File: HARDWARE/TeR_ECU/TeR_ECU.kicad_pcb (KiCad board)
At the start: 2 copper layers, 71 parts, among them IC1 MX34040NF2, J1 RJ45_Shielded, J2 RJ45_Shielded, J3 RJ45_Shielded, J4 Debug, Q1 ZXMN3F30FH, Q2 ZXMN3F30FH, SW1 RST, U1 SN65HVD230, U2 SN65HVD230, U3 STM32F446RETx, U4 TSR_1-24120, U5 TSR_1-2450, U6 LM1117MP-3.3, Y1 Crystal

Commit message: Latout empezado
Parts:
- moved IC1 163.1 mm to (160.7, 140.3)
- moved U3 130.2 mm to (151.7, 99.4)
- moved F1 128.8 mm to (190.7, 44.4)
- moved L2 128.5 mm to (187.6, 40.5)
- moved C18 128.5 mm to (186.0, 48.0)
- moved C19 128.5 mm to (186.0, 51.0)
- moved U2 88.0 mm to (126.5, 88.1), turned to 180 degrees
- moved JP2 82.0 mm to (120.5, 88.0), turned to 90 degrees
- moved R3 78.6 mm to (116.8, 90.0)
- moved D2 76.7 mm to (112.3, 88.4), turned to 180 degrees
- moved C4 74.0 mm to (124.8, 84.2)
- moved R4 72.8 mm to (116.6, 86.2), turned to 180 degrees
- moved U4 71.8 mm to (119.0, 53.5)
- moved J1 66.1 mm to (116.3, 130.0)
- moved J2 65.1 mm to (103.2, 110.3), turned to -90 degrees
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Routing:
- net +24V: track 0.00 -> 84.6 mm
- net /CAN2/CAN-: track 0.00 -> 22.6 mm
- net /CAN2/CAN+: track 0.00 -> 20.3 mm
- net GND: track 0.00 -> 14.3 mm, vias 0 -> 4
- net /CAN2/VREF: track 0.00 -> 12.4 mm, vias 0 -> 2
- net Net-(U5-Vin): track 0.00 -> 9.43 mm
- net +3.3V: track 0.00 -> 9.16 mm
- net Net-(C22-Pad1): track 0.00 -> 5.54 mm
- net Net-(JP2-B): track 0.00 -> 3.57 mm
- net Net-(JP2-A): track 0.00 -> 3.11 mm
- net +5V: track 0.00 -> 2.83 mm
- added copper zone on In1.Cu, net GND
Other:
- copper layers 2 -> 4

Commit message: Contuinuando con Layout, micro hecha
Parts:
- moved C8 148.5 mm to (155.9, 107.7)
- moved C9 147.9 mm to (159.9, 94.9), turned to 90 degrees
- moved C6 142.9 mm to (147.6, 107.5)
- moved C16 134.3 mm to (147.5, 90.9), turned to 180 degrees
- moved C5 134.1 mm to (143.4, 90.7), turned to -90 degrees
- moved C7 134.1 mm to (143.7, 95.8), turned to 90 degrees
- moved J4 127.5 mm to (159.4, 90.3), turned to -90 degrees
- moved C15 123.9 mm to (136.5, 96.3), turned to -90 degrees
- moved C14 123.5 mm to (136.5, 92.5), turned to -90 degrees
- moved FB1 122.0 mm to (142.1, 103.5), turned to -90 degrees
- moved R8 120.2 mm to (141.2, 98.6), turned to 180 degrees
- moved C10 118.2 mm to (143.6, 101.4), turned to -90 degrees
- moved C11 114.3 mm to (139.8, 102.4)
- moved C12 114.0 mm to (139.8, 103.6)
- moved Y1 107.0 mm to (139.7, 94.7), turned to -90 degrees
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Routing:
- net GND: track 14.3 -> 40.4 mm, vias 4 -> 9
- net +3.3V: track 9.16 -> 34.8 mm, vias 0 -> 2
- net /Micro/OSC_IN: track 0.00 -> 13.9 mm
- net +24V: track 84.6 -> 93.2 mm
- net /Micro/SWDIO: track 0.00 -> 7.99 mm
- net Net-(C15-Pad2): track 0.00 -> 6.14 mm
- net +3.3VADC: track 0.00 -> 6.00 mm
- net /Micro/OSC_OUT: track 0.00 -> 4.50 mm
- net /Micro/SWCLK: track 0.00 -> 3.45 mm
- added copper zone on In2.Cu, net +3.3V
- added copper zone on In2.Cu, net +5V
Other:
- board text added: "DBUG"

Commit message: Seguir Layout, falta señales
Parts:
- moved R7 150.5 mm to (166.6, 96.0), turned to 180 degrees
- moved R6 149.2 mm to (166.6, 87.4), turned to 180 degrees
- moved JP3 147.5 mm to (169.4, 90.1), turned to -90 degrees
- moved JP4 144.2 mm to (169.4, 93.5), turned to -90 degrees
- moved C13 125.9 mm to (133.7, 103.0), turned to 90 degrees
- moved R5 121.5 mm to (133.7, 99.4), turned to -90 degrees
- moved U1 100.6 mm to (125.4, 109.4), turned to 180 degrees
- moved SW1 99.8 mm to (130.4, 101.2), turned to 90 degrees
- moved C1 97.4 mm to (130.4, 109.5), turned to 90 degrees
- moved JP1 88.6 mm to (119.3, 109.4), turned to 90 degrees
- moved R1 87.8 mm to (115.7, 111.4)
- moved C3 87.4 mm to (121.7, 105.4), turned to 180 degrees
- moved D1 87.2 mm to (111.2, 109.3), turned to 180 degrees
- moved R2 85.8 mm to (115.6, 107.4), turned to 180 degrees
- moved C2 82.0 mm to (131.2, 86.8), turned to 90 degrees
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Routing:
- net /DBG_LED: track 0.00 -> 33.6 mm, vias 0 -> 2
- net +24V: track 93.2 -> 59.7 mm
- net +3.3V: track 34.8 -> 67.9 mm, vias 2 -> 9
- net GND: track 40.4 -> 72.4 mm, vias 9 -> 15
- net /IMP_LED: track 0.00 -> 30.7 mm, vias 0 -> 2
- net /CAN1/CAN-: track 0.00 -> 23.0 mm
- net /Micro/BOOT0: track 0.00 -> 22.0 mm, vias 0 -> 2
- net /CAN1/CAN+: track 0.00 -> 21.0 mm
- net /Micro/NRST: track 0.00 -> 19.1 mm, vias 0 -> 2
- net /Micro/BOOT1: track 0.00 -> 17.6 mm, vias 0 -> 2
- net /CAN1/VREF: track 0.00 -> 16.6 mm, vias 0 -> 2
- net Net-(SW1-B): track 0.00 -> 3.76 mm
- net Net-(JP1-B): track 0.00 -> 3.08 mm
- net Net-(JP1-A): track 0.00 -> 2.98 mm
- net Net-(JP3-C): track 0.00 -> 2.71 mm
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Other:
- board text added: "BOOT0"
- board text added: "BOOT1"

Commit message: avanzando
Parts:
- moved R13 140.8 mm to (152.6, 112.0), turned to 90 degrees
- moved Q1 140.2 mm to (156.3, 114.2)
- moved R14 134.6 mm to (145.4, 117.5)
- moved Q2 134.6 mm to (150.0, 120.0)
- moved R15 134.5 mm to (145.4, 120.5)
- moved R16 134.5 mm to (145.4, 123.3)
- moved R17 134.4 mm to (145.4, 125.8)
- moved R9 115.5 mm to (164.2, 99.3), turned to 180 degrees
- moved R11 113.6 mm to (164.3, 102.0), turned to 180 degrees
- moved R10 110.6 mm to (161.0, 98.5), turned to 90 degrees
- moved R12 109.1 mm to (160.8, 102.2), turned to -90 degrees
- moved L2 57.8 mm to (138.0, 70.1)
- moved F1 53.0 mm to (144.4, 70.2), turned to 180 degrees
- moved C19 52.3 mm to (135.8, 65.6), turned to 90 degrees
- moved C18 49.2 mm to (140.1, 65.5), turned to 90 degrees
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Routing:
- net GND: track 72.4 -> 82.0 mm, vias 15 -> 18
- net Net-(U4-Vin): track 0.00 -> 8.62 mm
- net Net-(C18-Pad1): track 0.00 -> 7.05 mm
- net /Micro/BOOT1: track 17.6 -> 24.5 mm
- net /Detección señales/BSPD_3V3: track 0.00 -> 6.77 mm
- net /Detección señales/TSMS_3V3: track 0.00 -> 6.07 mm
- net /Micro/BOOT0: track 22.0 -> 19.1 mm

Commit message: Falta poco
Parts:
- moved C21 58.5 mm to (121.5, 127.8), turned to -90 degrees
- moved U4 56.7 mm to (145.9, 123.8), turned to 180 degrees
- moved U6 54.8 mm to (115.8, 126.2), turned to 180 degrees
- moved C19 54.6 mm to (148.4, 118.8), turned to 0 degrees
- moved C18 53.2 mm to (137.7, 118.7), turned to 180 degrees
- moved C17 52.2 mm to (124.7, 123.8), turned to -90 degrees
- moved C20 51.1 mm to (121.5, 124.0), turned to -90 degrees
- moved L2 49.0 mm to (143.1, 118.8), turned to 180 degrees
- moved U5 48.6 mm to (128.4, 120.3), turned to -90 degrees
- moved R17 48.0 mm to (171.3, 85.3)
- moved R16 47.9 mm to (171.4, 83.0)
- moved R15 44.9 mm to (157.4, 77.3), turned to 180 degrees
- moved C22 44.8 mm to (115.4, 121.2), turned to 180 degrees
- moved F1 44.2 mm to (142.1, 114.3)
- moved L1 41.7 mm to (121.5, 119.2), turned to 180 degrees
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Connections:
- U3 pad 24: unconnected-(U3-PC4-Pad24) -> /Functions/BL
- U3 pad 25: unconnected-(U3-PC5-Pad25) -> /Functions/Horn
- U3 pad 52: /Functions/BL -> unconnected-(U3-PC11-Pad52)
- U3 pad 53: /Functions/Horn -> unconnected-(U3-PC12-Pad53)
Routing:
- net /CAN1/CAN-: track 23.0 -> 87.3 mm
- net /CAN1/CAN+: track 21.0 -> 77.2 mm
- net +24V: track 59.7 -> 23.5 mm, vias 0 -> 1
- net Net-(Q1-G): track 0.00 -> 7.77 mm
- net /Functions/Horn: track 0.00 -> 5.68 mm
- net /DBG_LED: track 33.6 -> 36.7 mm
- net /IMP_LED: track 30.7 -> 33.8 mm
- net /Micro/NRST: track 19.1 -> 21.4 mm
- net GND: track 82.0 -> 84.2 mm, vias 18 -> 19
- net Net-(U4-Vin): track 8.62 -> 7.57 mm
- net +3.3V: track 67.5 -> 67.7 mm, vias 9 -> 10
- added copper zone on In2.Cu, net +24V

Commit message: Falta Conector
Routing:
- net /CAN1/CAN_TX: track 0.00 -> 36.1 mm
- net /CAN1/CAN_RX: track 0.00 -> 34.1 mm, vias 0 -> 2
- net +24V: track 23.5 -> 56.6 mm
- net GND: track 84.2 -> 102.8 mm, vias 19 -> 27
- net +5V: track 2.83 -> 5.46 mm, vias 0 -> 1
- net /Micro/BOOT1: track 24.5 -> 23.5 mm
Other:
- board text added: "CAN+"
- board text added: "CAN-"

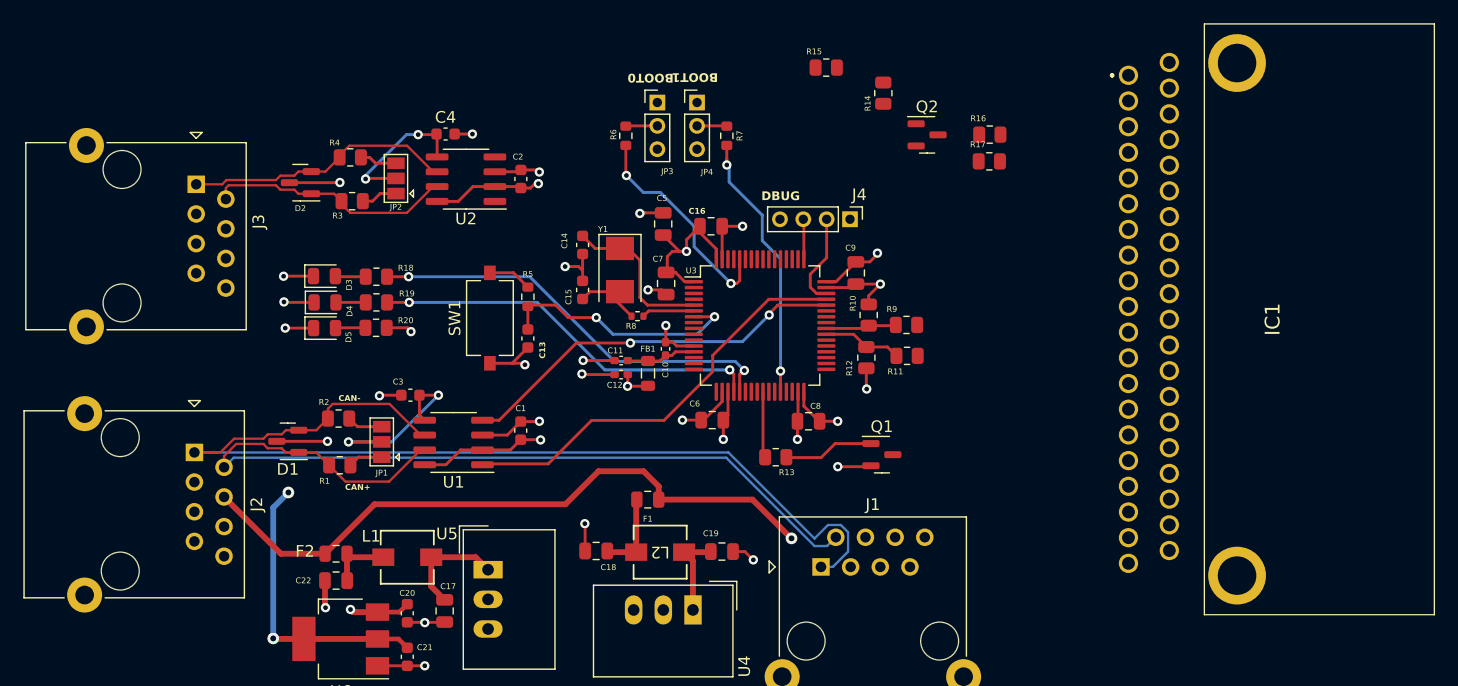
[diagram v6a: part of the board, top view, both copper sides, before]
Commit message: Falta pinear conector
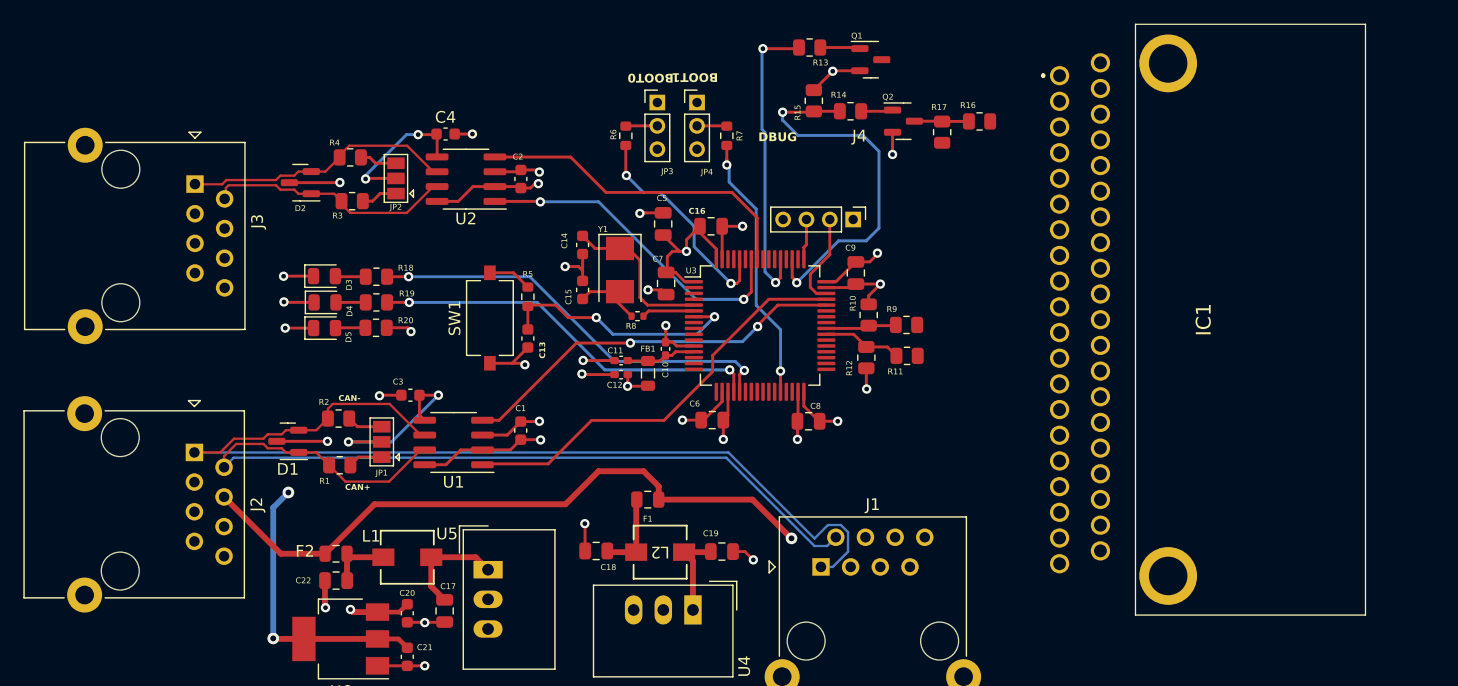
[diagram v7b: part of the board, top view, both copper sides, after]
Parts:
- moved R13 35.2 mm to (155.9, 75.6)
- moved Q1 33.8 mm to (161.2, 76.6)
- moved IC1 5.90 mm to (189.7, 98.9)
- moved R17 4.75 mm to (167.3, 82.8), turned to -90 degrees
- moved R14 3.21 mm to (159.4, 81.0), turned to 180 degrees
- moved R15 3.03 mm to (156.3, 80.2), turned to 90 degrees
- moved Q2 2.34 mm to (164.0, 81.9)
- moved R16 1.43 mm to (170.5, 81.9)
- moved J4 0.27 mm to (159.7, 90.3)
- moved J3 0.11 mm to (103.3, 87.3)
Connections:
- U3 pad 24: /Functions/BL -> unconnected-(U3-PC4-Pad24)
- U3 pad 25: /Functions/Horn -> unconnected-(U3-PC5-Pad25)
- U3 pad 33: /CAN2/CAN_TX -> unconnected-(U3-PB12-Pad33)
- U3 pad 34: /CAN2/CAN_RX -> unconnected-(U3-PB13-Pad34)
- U3 pad 51: unconnected-(U3-PC10-Pad51) -> /Functions/BL
- U3 pad 53: unconnected-(U3-PC12-Pad53) -> /Functions/Horn
- U3 pad 57: unconnected-(U3-PB5-Pad57) -> /CAN2/CAN_RX
- U3 pad 58: unconnected-(U3-PB6-Pad58) -> /CAN2/CAN_TX
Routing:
- net /Functions/BL: track 0.00 -> 33.1 mm, vias 0 -> 2
- net /CAN2/CAN_TX: track 0.00 -> 28.6 mm, vias 0 -> 2
- net /CAN2/CAN_RX: track 0.00 -> 28.2 mm
- net /Functions/Horn: track 5.68 -> 25.9 mm, vias 0 -> 2
- net Net-(Q2-D): track 0.00 -> 4.68 mm
- net Net-(Q1-G): track 7.77 -> 3.43 mm
- net GND: track 102.8 -> 106.6 mm, vias 27 -> 28
- net Net-(Q2-G): track 0.00 -> 2.73 mm

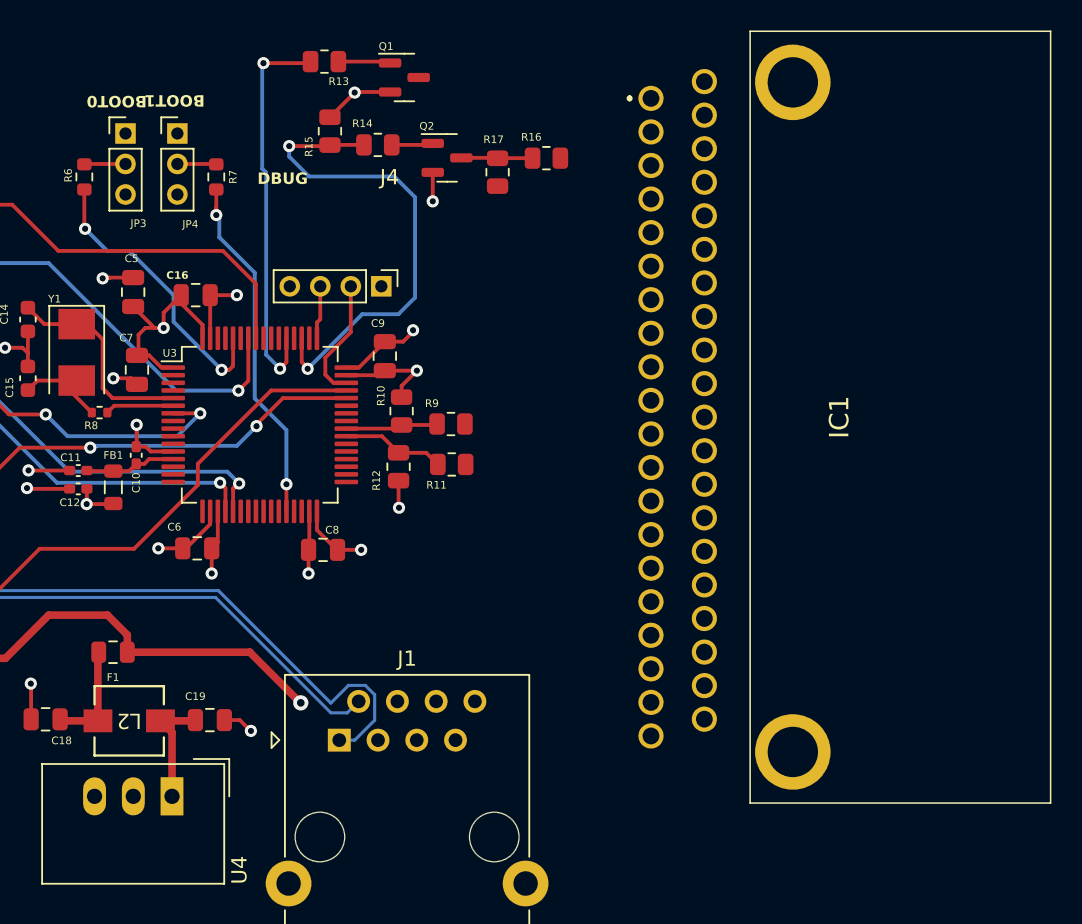
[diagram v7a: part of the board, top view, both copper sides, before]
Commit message: Falata routear señales al conector
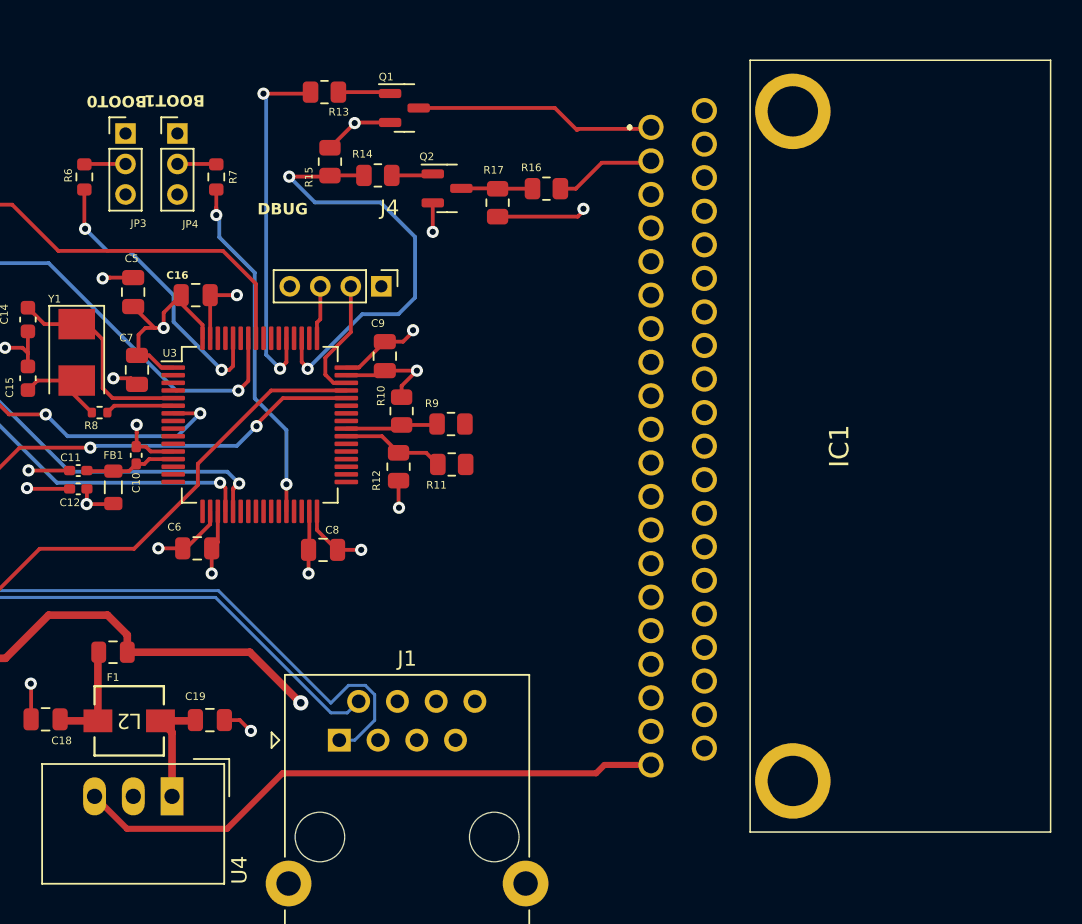
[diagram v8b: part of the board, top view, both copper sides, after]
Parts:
- moved Q1 2.00 mm to (161.2, 78.6)
- moved Q2 2.00 mm to (164.0, 83.9)
- moved R13 2.00 mm to (155.9, 77.6)
- moved R14 2.00 mm to (159.4, 83.0)
- moved R15 2.00 mm to (156.3, 82.2)
- moved R16 2.00 mm to (170.5, 83.9)
- moved R17 2.00 mm to (167.3, 84.8)
- moved IC1 1.90 mm to (189.7, 100.8)
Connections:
- IC1 pad 1: /Conector/BSPD_5V -> /Conector/Horn_GND
- IC1 pad 10: GND -> unconnected-(IC1-Pad10)
- IC1 pad 11: +24V -> unconnected-(IC1-Pad11)
- IC1 pad 12: +24V -> unconnected-(IC1-Pad12)
- IC1 pad 2: /Conector/TSMS_24V -> /Conector/BL_GND
- IC1 pad 20: unconnected-(IC1-Pad20) -> +12V
- IC1 pad 21: unconnected-(IC1-Pad21) -> +24V
- IC1 pad 22: +12V -> +24V
- IC1 pad 24: GND -> unconnected-(IC1-Pad24)
- IC1 pad 27: +5V -> unconnected-(IC1-Pad27)
- IC1 pad 28: +5V -> unconnected-(IC1-Pad28)
- IC1 pad 29: +5V -> unconnected-(IC1-Pad29)
- IC1 pad 3: /Conector/BL_GND -> +24V
- IC1 pad 30: GND -> unconnected-(IC1-Pad30)
- IC1 pad 31: GND -> unconnected-(IC1-Pad31)
- IC1 pad 32: GND -> unconnected-(IC1-Pad32)
- IC1 pad 39: +24V -> GND
- IC1 pad 4: +24V -> unconnected-(IC1-Pad4)
- IC1 pad 5: /Conector/Horn_GND -> unconnected-(IC1-Pad5)
- IC1 pad 6: +24V -> unconnected-(IC1-Pad6)
- IC1 pad 7: +24V -> unconnected-(IC1-Pad7)
- IC1 pad 8: GND -> unconnected-(IC1-Pad8)
- IC1 pad 9: GND -> unconnected-(IC1-Pad9)
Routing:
- net +12V: track 0.00 -> 39.1 mm
- net /Conector/Horn_GND: track 0.00 -> 15.9 mm
- net /Conector/BL_GND: track 0.00 -> 6.65 mm
- net +24V: track 56.6 -> 62.8 mm, vias 1 -> 2
- net /Functions/BL: track 33.1 -> 30.4 mm
- net /Functions/Horn: track 25.9 -> 24.0 mm
